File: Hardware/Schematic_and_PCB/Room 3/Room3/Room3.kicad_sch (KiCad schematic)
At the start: 17 parts, among them Q1 BC557, Q2 BC557, Q3 BC557, SW1 SW_Push

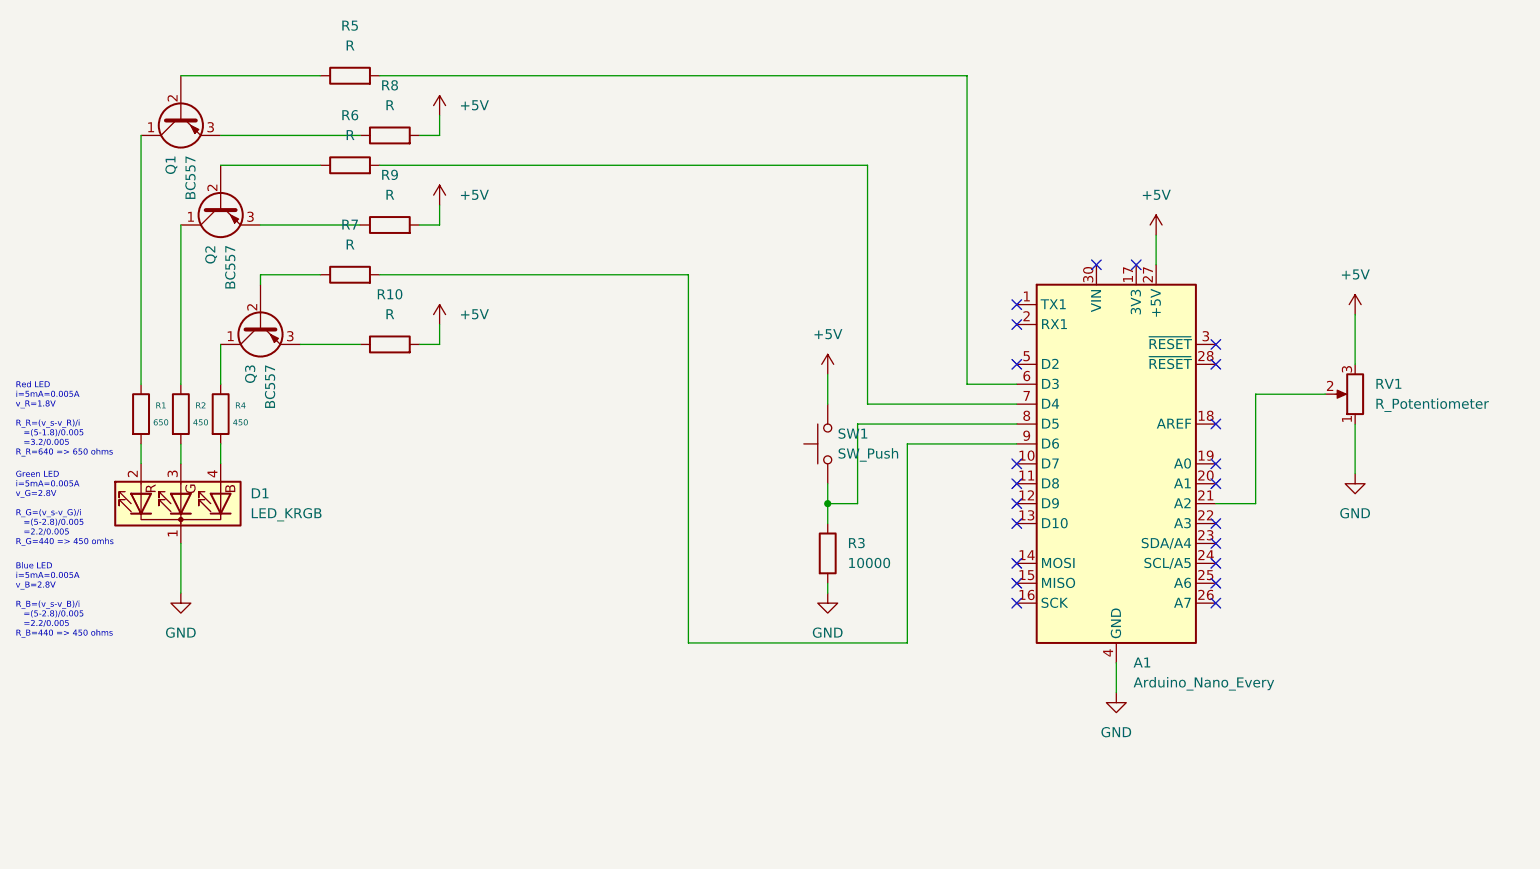
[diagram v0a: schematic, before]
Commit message: Update room 3 with calculations
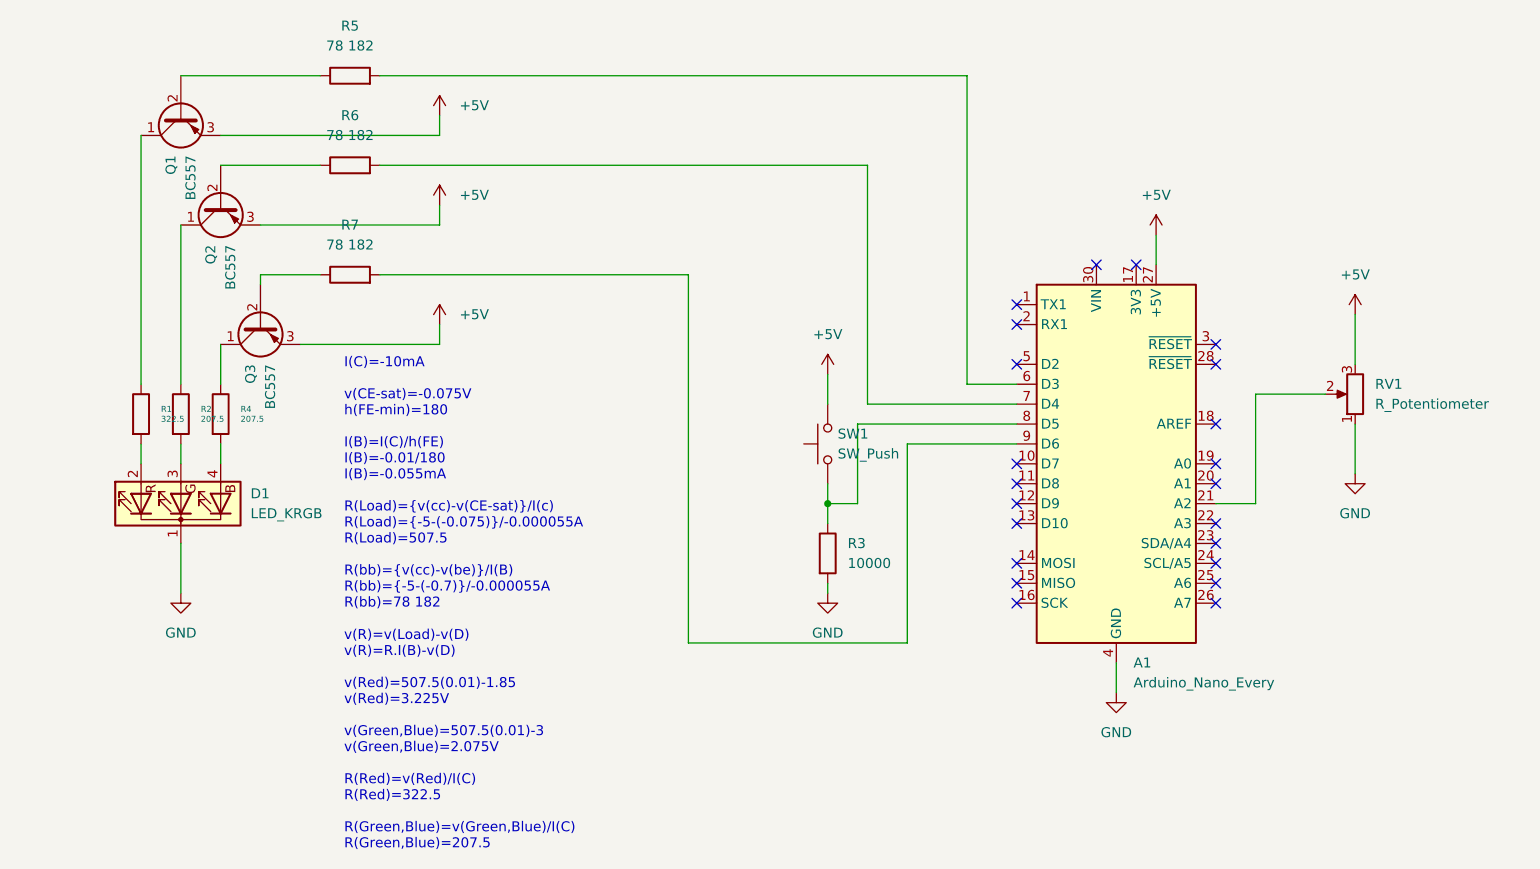
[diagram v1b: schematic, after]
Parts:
- removed R10, R8, R9: R, symbol Device:R
- R1: value 650 -> 322.5
- R2, R4: value 450 -> 207.5
- R5, R6, R7: value R -> 78 182
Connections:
- net +5V: now also Q1.3 (E), Q2.3 (E), Q3.3 (E)
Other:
- note added: "I(C)=-10mA v(CE-sat)=-0.075V h(FE-min)=180 I(B)=I(C)/h(FE) I(B)=-0.01/180 I(B)=-0.055mA R(Load)={v(cc)-v(CE-sat)}/I(c) R(Load)={-5-(-0.075)}/-0.000055A R(Load)=507.5 R(bb)={v(cc)-v(be)}/I(B) R(bb)={-5-(-0.7)}/-0.000055A R(bb)=78 182"
- note added: "v(R)=v(Load)-v(D) v(R)=R.I(B)-v(D) v(Red)=507.5(0.01)-1.85 v(Red)=3.225V v(Green,Blue)=507.5(0.01)-3 v(Green,Blue)=2.075V R(Red)=v(Red)/I(C) R(Red)=322.5 R(Green,Blue)=v(Green,Blue)/I(C) R(Green,Blue)=207.5"
- note removed: "Blue LED i=5mA=0.005A v_B=2.8V R_B=(v_s-v_B)/i =(5-2.8)/0.005 =2.2/0.005 R_B=440 => 450 ohms"
- note removed: "Green LED i=5mA=0.005A v_G=2.8V R_G=(v_s-v_G)/i =(5-2.8)/0.005 =2.2/0.005 R_G=440 => 450 omhs"
- note removed: "Red LED i=5mA=0.005A v_R=1.8V R_R=(v_s-v_R)/i =(5-1.8)/0.005 =3.2/0.005 R_R=640 => 650 ohms"

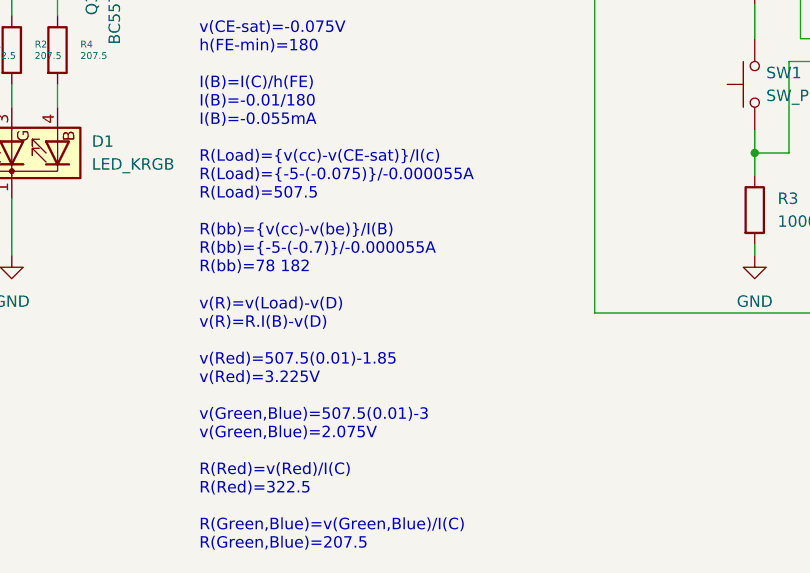
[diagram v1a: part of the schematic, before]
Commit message: Updated calculations
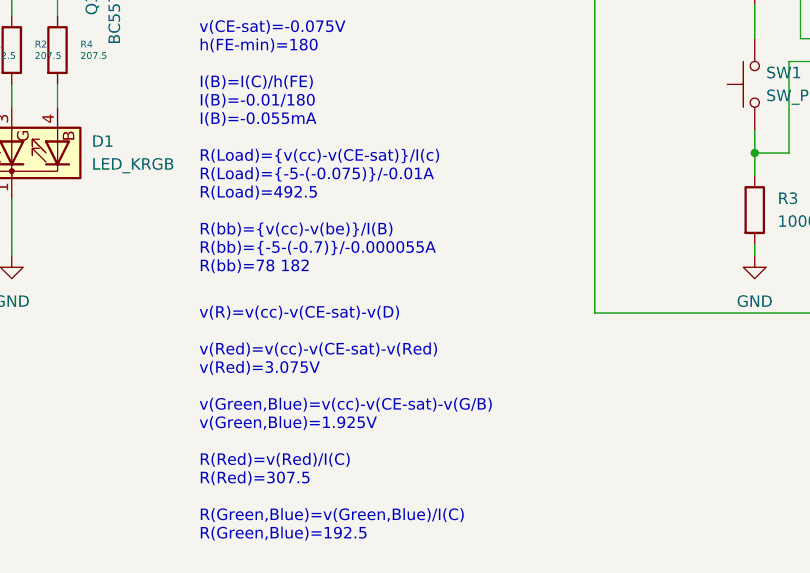
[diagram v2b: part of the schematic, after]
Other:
- note added: "I(C)=-10mA v(CE-sat)=-0.075V h(FE-min)=180 I(B)=I(C)/h(FE) I(B)=-0.01/180 I(B)=-0.055mA R(Load)={v(cc)-v(CE-sat)}/I(c) R(Load)={-5-(-0.075)}/-0.01A R(Load)=492.5 R(bb)={v(cc)-v(be)}/I(B) R(bb)={-5-(-0.7)}/-0.000055A R(bb)=78 182"
- note added: "v(R)=v(cc)-v(CE-sat)-v(D) v(Red)=v(cc)-v(CE-sat)-v(Red) v(Red)=3.075V v(Green,Blue)=v(cc)-v(CE-sat)-v(G/B) v(Green,Blue)=1.925V R(Red)=v(Red)/I(C) R(Red)=307.5 R(Green,Blue)=v(Green,Blue)/I(C) R(Green,Blue)=192.5"
- note removed: "I(C)=-10mA v(CE-sat)=-0.075V h(FE-min)=180 I(B)=I(C)/h(FE) I(B)=-0.01/180 I(B)=-0.055mA R(Load)={v(cc)-v(CE-sat)}/I(c) R(Load)={-5-(-0.075)}/-0.000055A R(Load)=507.5 R(bb)={v(cc)-v(be)}/I(B) R(bb)={-5-(-0.7)}/-0.000055A R(bb)=78 182"
- note removed: "v(R)=v(Load)-v(D) v(R)=R.I(B)-v(D) v(Red)=507.5(0.01)-1.85 v(Red)=3.225V v(Green,Blue)=507.5(0.01)-3 v(Green,Blue)=2.075V R(Red)=v(Red)/I(C) R(Red)=322.5 R(Green,Blue)=v(Green,Blue)/I(C) R(Green,Blue)=207.5"
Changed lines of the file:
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@@
 		)
 	)
-	(text "v(R)=v(Load)-v(D)\nv(R)=R.I(B)-v(D)\n\nv(Red)=507.5(0.01)-1.85\nv(Red)=3.225V\n\nv(Green,Blue)=507.5(0.01)-3\nv(Green,Blue)=2.075V\n\nR(Red)=v(Red)/I(C)\nR(Red)=322.5\n\nR(Green,Blue)=v(Green,Blue)/I(C)\nR(Green,Blue)=207.5"
+	(text "v(R)=v(cc)-v(CE-sat)-v(D)\n\nv(Red)=v(cc)-v(CE-sat)-v(Red)\nv(Red)=3.075V\n\nv(Green,Blue)=v(cc)-v(CE-sat)-v(G/B)\nv(Green,Blue)=1.925V\n\nR(Red)=v(Red)/I(C)\nR(Red)=307.5\n\nR(Green,Blue)=v(Green,Blue)/I(C)\nR(Green,Blue)=192.5"
 		(exclude_from_sim no)
 		(at 55.118 135.636 0)
@@
 		)
 	)
-	(text "I(C)=-10mA\n\nv(CE-sat)=-0.075V\nh(FE-min)=180\n\nI(B)=I(C)/h(FE)\nI(B)=-0.01/180\nI(B)=-0.055mA\n\nR(Load)={v(cc)-v(CE-sat)}/I(c)\nR(Load)={-5-(-0.075)}/-0.000055A\nR(Load)=507.5\n\nR(bb)={v(cc)-v(be)}/I(B)\nR(bb)={-5-(-0.7)}/-0.000055A\nR(bb)=78 182\n"
+	(text "I(C)=-10mA\n\nv(CE-sat)=-0.075V\nh(FE-min)=180\n\nI(B)=I(C)/h(FE)\nI(B)=-0.01/180\nI(B)=-0.055mA\n\nR(Load)={v(cc)-v(CE-sat)}/I(c)\nR(Load)={-5-(-0.075)}/-0.01A\nR(Load)=492.5\n\nR(bb)={v(cc)-v(be)}/I(B)\nR(bb)={-5-(-0.7)}/-0.000055A\nR(bb)=78 182\n"
 		(exclude_from_sim no)
 		(at 55.118 102.87 0)

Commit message: Update Room3.kicad_sch
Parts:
- R5: value 78 182 -> 78k
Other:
- note added: "v(R)=v(cc)-v(CE-sat)-v(D)(general Equation) v(Red)=v(cc)-v(CE-sat)-v(r) v(r)= Voltage drop of the red diode v(Red)=3.075V v(Green,Blue)=v(cc)-v(CE-sat)-v(G/B) v(Green,Blue)=1.925V R(Red)=v(Red)/I(C) R(Red)=307.5 R(Green,Blue)=v(Green,Blue)/I(C) R(Green,Blue)=192.5"
- note removed: "v(R)=v(cc)-v(CE-sat)-v(D) v(Red)=v(cc)-v(CE-sat)-v(Red) v(Red)=3.075V v(Green,Blue)=v(cc)-v(CE-sat)-v(G/B) v(Green,Blue)=1.925V R(Red)=v(Red)/I(C) R(Red)=307.5 R(Green,Blue)=v(Green,Blue)/I(C) R(Green,Blue)=192.5"
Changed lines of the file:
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@@
 		)
 	)
-	(text "v(R)=v(cc)-v(CE-sat)-v(D)\n\nv(Red)=v(cc)-v(CE-sat)-v(Red)\nv(Red)=3.075V\n\nv(Green,Blue)=v(cc)-v(CE-sat)-v(G/B)\nv(Green,Blue)=1.925V\n\nR(Red)=v(Red)/I(C)\nR(Red)=307.5\n\nR(Green,Blue)=v(Green,Blue)/I(C)\nR(Green,Blue)=192.5"
+	(text "v(R)=v(cc)-v(CE-sat)-v(D)(general Equation)\n\nv(Red)=v(cc)-v(CE-sat)-v(r)\nv(r)= Voltage drop of the red diode\nv(Red)=3.075V\n\nv(Green,Blue)=v(cc)-v(CE-sat)-v(G/B)\nv(Green,Blue)=1.925V\n\nR(Red)=v(Red)/I(C)\nR(Red)=307.5\n\nR(Green,Blue)=v(Green,Blue)/I(C)\nR(Green,Blue)=192.5"
 		(exclude_from_sim no)
 		(at 55.118 135.636 0)
@@
 			)
 		)
-		(property "Value" "78 182"
+		(property "Value" "78k"
 			(at 55.88 46.99 90)
 			(effects
